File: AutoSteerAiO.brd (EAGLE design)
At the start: 114.3 x 99.1 mm, 81 parts, among them IC2 MMA8452Q, J4 CONNECTOR 1x5 PINS, K4 CB1A-P-12V

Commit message: Add files via upload
silkscreen edit
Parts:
- moved D3 1.91 mm to (36.2, 90.8)
- moved D2 0.63 mm to (42.5, 90.8)
- moved INT 0.45 mm to (27.3, 80.6)
- moved PCB1 0.44 mm to (48.1, 32.4)
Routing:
- net GND: track 460.9 -> 463.2 mm, vias 85 -> 79
- net N$26: track 77.2 -> 75.7 mm
- net SDA: track 98.8 -> 97.9 mm
- net SCL: track 99.0 -> 98.1 mm

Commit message: Add files via upload
silkscreen edit
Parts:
- moved C11 0.64 mm to (42.5, 65.4)
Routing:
- net +15V: track 131.5 -> 127.8 mm
- net +5V: track 233.9 -> 232.1 mm
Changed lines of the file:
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@@
 <drawing>
 <settings>
-<setting alwaysvectorfont="yes"/>
+<setting alwaysvectorfont="no"/>
 <setting keepoldvectorfont="yes"/>
 <setting verticaltext="up"/>
@@
 <text x="39.37" y="30.226" size="1.016" layer="25" font="vector" ratio="12" rot="R180" align="center">USB</text>
 <text x="40.64" y="114.3" size="2.54" layer="25" font="vector" ratio="14" rot="R180" align="center">AGOpenGPS</text>
-<text x="41.91" y="61.595" size="0.8128" layer="25" font="vector" ratio="12" rot="R180" align="center">.1uF</text>
+<text x="42.545" y="61.595" size="0.8128" layer="25" font="vector" ratio="12" rot="R180" align="center">.1uF</text>
 <text x="54.61" y="33.02" size="0.7112" layer="25" font="vector" ratio="10" align="center">3V</text>
 <text x="67.31" y="33.02" size="0.7112" layer="25" font="vector" ratio="10" align="center">GND</text>
@@
 <attribute name="OC_NEWARK" value="unknown" x="116.84" y="114.3" size="1.778" layer="27" display="off"/>
 </element>
-<element name="C11" library="resistor" library_urn="urn:adsk.eagle:library:348" package="C050-024X044" package3d_urn="urn:adsk.eagle:package:23643/1" value=".1uF" x="41.91" y="65.405" smashed="yes" rot="R270">
-<attribute name="MF" value="" x="41.91" y="65.405" size="1.778" layer="27" rot="R270" display="off"/>
-<attribute name="MPN" value="" x="41.91" y="65.405" size="1.778" layer="27" rot="R270" display="off"/>
-<attribute name="NAME" x="41.91" y="69.215" size="0.8128" layer="25" font="vector" ratio="12" rot="R180" align="center"/>
-<attribute name="OC_NEWARK" value="unknown" x="41.91" y="65.405" size="1.778" layer="27" rot="R270" display="off"/>
+<element name="C11" library="resistor" library_urn="urn:adsk.eagle:library:348" package="C050-024X044" package3d_urn="urn:adsk.eagle:package:23643/1" value=".1uF" x="42.545" y="65.405" smashed="yes" rot="R270">
+<attribute name="MF" value="" x="42.545" y="65.405" size="1.778" layer="27" rot="R270" display="off"/>
+<attribute name="MPN" value="" x="42.545" y="65.405" size="1.778" layer="27" rot="R270" display="off"/>
+<attribute name="NAME" x="42.545" y="69.215" size="0.8128" layer="25" font="vector" ratio="12" rot="R180" align="center"/>
+<attribute name="OC_NEWARK" value="unknown" x="42.545" y="65.405" size="1.778" layer="27" rot="R270" display="off"/>
 </element>
 <element name="C12" library="resistor" library_urn="urn:adsk.eagle:library:348" package="C050-024X044" package3d_urn="urn:adsk.eagle:package:23643/1" value=".1uF" x="50.8" y="33.655" smashed="yes" rot="R270">
@@
 <attribute name="CYTRON-PC" value="CN-2600PS-05" x="117.475" y="68.58" size="1.778" layer="27" rot="R90" display="off"/>
 <attribute name="DESC" value="2600 PCB Connector" x="117.475" y="68.58" size="1.778" layer="27" rot="R90" display="off"/>
+<attribute name="LABEL" value="" x="120.396" y="67.183" size="0.762" layer="51" font="vector" ratio="15" rot="R90" align="top-left"/>
 <attribute name="LABEL" value="" x="120.396" y="67.183" size="0.762" layer="21" font="vector" ratio="15" rot="R90" align="top-left"/>
-<attribute name="LABEL" value="" x="120.396" y="67.183" size="0.762" layer="51" font="vector" ratio="15" rot="R90" align="top-left"/>
 <attribute name="LABEL" value="" x="117.475" y="68.58" size="1.778" layer="27" rot="R90" display="off"/>
 <attribute name="MF" value="" x="117.475" y="68.58" size="1.778" layer="27" rot="R90" display="off"/>
@@
 <contactref element="+5V1" pad="1"/>
 <wire x1="10.16" y1="31.3055" x2="10.16" y2="70.8025" width="0.6096" layer="1"/>
-<wire x1="41.91" y1="36.83" x2="41.91" y2="62.865" width="0.6096" layer="1"/>
-<wire x1="41.91" y1="36.83" x2="30.48" y2="25.4" width="0.6096" layer="1"/>
-<wire x1="46.7995" y1="62.865" x2="41.91" y2="62.865" width="0.508" layer="1"/>
+<wire x1="42.545" y1="37.465" x2="42.545" y2="62.865" width="0.6096" layer="1"/>
+<wire x1="42.545" y1="37.465" x2="30.48" y2="25.4" width="0.6096" layer="1"/>
+<wire x1="46.7995" y1="62.865" x2="42.545" y2="62.865" width="0.508" layer="1"/>
 <contactref element="PS2" pad="3"/>
 <contactref element="C10" pad="2"/>
@@
 <wire x1="14.9225" y1="75.565" x2="10.16" y2="70.8025" width="0.6096" layer="1"/>
 <wire x1="15.0013125" y1="88.9" x2="12.7" y2="88.9" width="0.4064" layer="1"/>
-<wire x1="18.6081125" y1="92.5068" x2="15.0013125" y2="88.9" width="0.4064" layer="1"/>
-<wire x1="51.435" y1="80.01" x2="38.9382" y2="92.5068" width="0.4064" layer="1"/>
-<wire x1="38.9382" y1="92.5068" x2="18.6081125" y2="92.5068" width="0.4064" layer="1"/>
+<wire x1="16.9063125" y1="90.805" x2="15.0013125" y2="88.9" width="0.4064" layer="1"/>
+<wire x1="50.165" y1="80.01" x2="39.37" y2="90.805" width="0.4064" layer="1"/>
+<wire x1="39.37" y1="90.805" x2="16.9063125" y2="90.805" width="0.4064" layer="1"/>
 <wire x1="61.9125" y1="80.01" x2="63.5" y2="81.5975" width="0.4064" layer="1"/>
-<wire x1="51.435" y1="80.01" x2="61.9125" y2="80.01" width="0.4064" layer="1"/>
+<wire x1="50.165" y1="80.01" x2="61.9125" y2="80.01" width="0.4064" layer="1"/>
 <contactref element="C16" pad="+"/>
 <wire x1="12.7" y1="85.09" x2="20.28" y2="85.09" width="0.8128" layer="1"/>
@@
 <via x="15.24" y="57.15" extent="1-16" drill="0.508"/>
 <via x="16.51" y="22.86" extent="1-16" drill="0.508"/>
-<via x="33.655" y="50.8" extent="1-16" drill="0.508"/>
+<via x="33.655" y="48.895" extent="1-16" drill="0.508"/>
 <via x="58.42" y="25.4" extent="1-16" drill="0.508"/>
-<via x="39.37" y="78.105" extent="1-16" drill="0.508"/>
+<via x="39.37" y="78.74" extent="1-16" drill="0.508"/>
 <contactref element="J4" pad="1"/>
 <contactref element="JP1" pad="1"/>
@@
 <wire x1="117.475" y1="68.58" x2="120.015" y2="68.58" width="0.6096" layer="16"/>
 <wire x1="117.475" y1="85.09" x2="120.015" y2="85.09" width="0.6096" layer="16"/>
-<via x="38.735" y="36.83" extent="1-16" drill="0.508"/>
-<via x="38.735" y="22.86" extent="1-16" drill="0.508"/>
+<via x="39.37" y="36.83" extent="1-16" drill="0.508"/>
+<via x="39.37" y="22.86" extent="1-16" drill="0.508"/>
 <polygon width="0" layer="16" isolate="0.3556" thermals="no">
 <vertex x="120.65" y="63.5"/>
@@
 <vertex x="120.65" y="30.48"/>
 </polygon>
-<wire x1="46.7995" y1="67.945" x2="41.91" y2="67.945" width="0.6096" layer="16"/>
-<wire x1="41.91" y1="67.945" x2="36.83" y2="62.865" width="0.6096" layer="16"/>
-<wire x1="36.83" y1="62.865" x2="31.5595" y2="62.865" width="0.6096" layer="16"/>
+<wire x1="46.7995" y1="67.945" x2="42.545" y2="67.945" width="0.6096" layer="16"/>
+<wire x1="42.545" y1="67.945" x2="37.465" y2="62.865" width="0.6096" layer="16"/>
+<wire x1="37.465" y1="62.865" x2="31.5595" y2="62.865" width="0.6096" layer="16"/>
 <wire x1="31.5595" y1="62.865" x2="31.5341" y2="62.8904" width="0.6096" layer="16"/>
 <wire x1="31.5341" y1="62.8904" x2="22.8854" y2="62.8904" width="0.6096" layer="16"/>
@@
 <wire x1="67.31" y1="36.195" x2="50.8" y2="36.195" width="0.6096" layer="16"/>
 <wire x1="67.31" y1="31.115" x2="67.31" y2="36.195" width="0.6096" layer="16"/>
-<via x="43.815" y="50.8" extent="1-16" drill="0.508"/>
+<via x="44.45" y="48.895" extent="1-16" drill="0.508"/>
 <via x="113.03" y="22.86" extent="1-16" drill="0.508"/>
 <via x="40.64" y="111.125" extent="1-16" drill="0.508"/>
@@
 <wire x1="16.51" y1="60.325" x2="16.51" y2="67.945" width="0.508" layer="1"/>
 <wire x1="16.51" y1="67.945" x2="17.78" y2="69.215" width="0.508" layer="1"/>
-<wire x1="42.545" y1="85.725" x2="38.2016" y2="90.0684" width="0.8128" layer="1"/>
-<wire x1="38.2016" y1="90.0684" x2="25.3297125" y2="90.0684" width="0.8128" layer="1"/>
-<wire x1="25.3297125" y1="90.0684" x2="23.495" y2="88.2336875" width="0.8128" layer="1"/>
+<wire x1="42.545" y1="85.725" x2="40.64" y2="87.63" width="0.8128" layer="1"/>
+<wire x1="40.64" y1="87.63" x2="25.7488125" y2="87.63" width="0.8128" layer="1"/>
+<wire x1="25.7488125" y1="87.63" x2="23.495" y2="85.3761875" width="0.8128" layer="1"/>
 <polygon width="0" layer="16" thermals="no">
 <vertex x="74.295" y="85.09"/>
@@
 <vertex x="86.995" y="85.09"/>
 </polygon>
-<wire x1="23.495" y1="88.2336875" x2="23.495" y2="73.66" width="0.8128" layer="1"/>
+<wire x1="23.495" y1="85.3761875" x2="23.495" y2="73.66" width="0.8128" layer="1"/>
 <wire x1="23.495" y1="73.66" x2="21.2725" y2="73.66" width="0.6096" layer="1"/>
 <wire x1="21.2725" y1="73.66" x2="17.78" y2="70.1675" width="0.6096" layer="1"/>

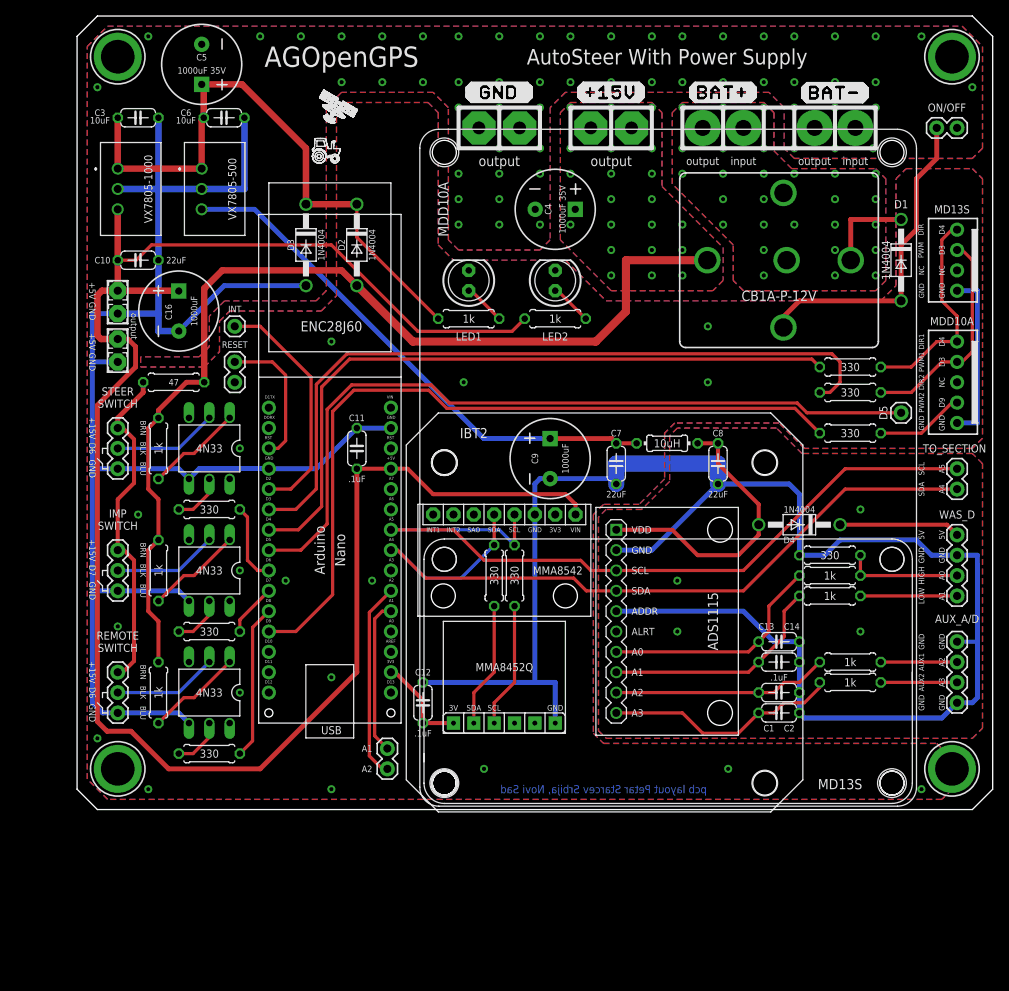
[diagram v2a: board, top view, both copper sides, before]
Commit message: Add files via upload
Added MD10C driver
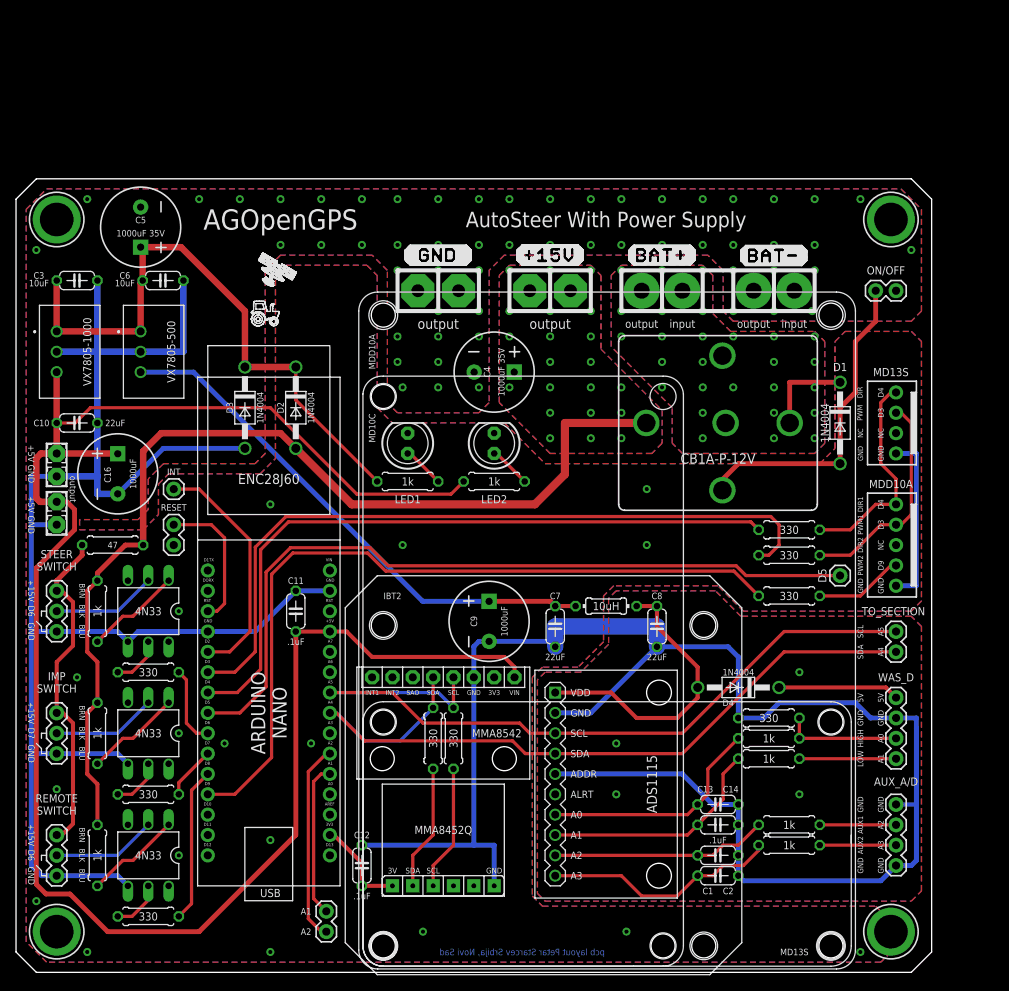
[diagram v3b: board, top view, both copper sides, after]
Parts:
- added U$3: MD10C, #Motor Drivers:MD10C
- moved U$1 99.4 mm to (45.8, 3.30), turned to 90 degrees
- moved +5V 21.7 mm to (5.08, 58.7)
- moved +5V1 21.7 mm to (5.08, 64.8)
- moved C10 21.7 mm to (7.62, 68.6)
- moved C3 21.7 mm to (7.62, 86.4)
- moved C6 21.7 mm to (18.4, 86.4)
- moved C9 21.7 mm to (59.1, 43.8)
- moved D1 21.7 mm to (102.9, 68.6)
- moved D2 21.7 mm to (34.9, 70.5)
- moved D3 21.7 mm to (28.6, 70.5)
- moved JP1 21.7 mm to (109.9, 68.6)
- moved K4 21.7 mm to (87.6, 68.6)
- moved L1 21.7 mm to (73.7, 45.7)
- moved PS1 21.7 mm to (16.8, 77.5)
- moved PS2 21.7 mm to (6.35, 77.5)
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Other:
- board text added: "MD10C"
- board text removed: "ENC28J60"

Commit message: Add files via upload
added MD10C holes
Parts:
- moved R10 0.64 mm to (94.0, 26.0)
- moved R11 0.64 mm to (94.0, 28.6)
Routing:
- net HIGH.: track 14.6 -> 15.5 mm
- net LOW: track 28.7 -> 28.0 mm
- net HIGH: track 28.7 -> 28.0 mm
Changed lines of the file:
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@@
 <drawing>
 <settings>
-<setting alwaysvectorfont="yes"/>
+<setting alwaysvectorfont="no"/>
 <setting keepoldvectorfont="yes"/>
 <setting verticaltext="up"/>
 </settings>
-<grid distance="50" unitdist="mil" unit="mm" style="lines" multiple="1" display="no" altdistance="5" altunitdist="mil" altunit="mil"/>
+<grid distance="50" unitdist="mil" unit="mil" style="lines" multiple="1" display="yes" altdistance="25" altunitdist="mil" altunit="mil"/>
 <layers>
 <layer number="1" name="Top" color="4" fill="1" visible="yes" active="yes"/>
@@
 <attribute name="VALUE" x="96.52" y="52.07" size="1.016" layer="25" font="vector" ratio="12" rot="R180" align="center"/>
 </element>
-<element name="R10" library="resistor" library_urn="urn:adsk.eagle:library:348" package="0207/7" package3d_urn="urn:adsk.eagle:package:23493/2" value="1k" x="93.98" y="26.67" smashed="yes" rot="R180">
-<attribute name="MF" value="" x="93.98" y="26.67" size="1.778" layer="27" rot="R180" display="off"/>
-<attribute name="MPN" value="" x="93.98" y="26.67" size="1.778" layer="27" rot="R180" display="off"/>
-<attribute name="OC_NEWARK" value="unknown" x="93.98" y="26.67" size="1.778" layer="27" rot="R180" display="off"/>
-<attribute name="VALUE" x="93.98" y="26.67" size="1.016" layer="25" font="vector" ratio="12" align="center"/>
-</element>
-<element name="R11" library="resistor" library_urn="urn:adsk.eagle:library:348" package="0207/7" package3d_urn="urn:adsk.eagle:package:23493/2" value="1k" x="93.98" y="29.21" smashed="yes" rot="R180">
-<attribute name="MF" value="" x="93.98" y="29.21" size="1.778" layer="27" rot="R180" display="off"/>
-<attribute name="MPN" value="" x="93.98" y="29.21" size="1.778" layer="27" rot="R180" display="off"/>
-<attribute name="OC_NEWARK" value="unknown" x="93.98" y="29.21" size="1.778" layer="27" rot="R180" display="off"/>
-<attribute name="VALUE" x="93.98" y="29.21" size="1.016" layer="25" font="vector" ratio="12" align="center"/>
+<element name="R10" library="resistor" library_urn="urn:adsk.eagle:library:348" package="0207/7" package3d_urn="urn:adsk.eagle:package:23493/2" value="1k" x="93.98" y="26.035" smashed="yes" rot="R180">
+<attribute name="MF" value="" x="93.98" y="26.035" size="1.778" layer="27" rot="R180" display="off"/>
+<attribute name="MPN" value="" x="93.98" y="26.035" size="1.778" layer="27" rot="R180" display="off"/>
+<attribute name="OC_NEWARK" value="unknown" x="93.98" y="26.035" size="1.778" layer="27" rot="R180" display="off"/>
+<attribute name="VALUE" x="93.98" y="26.035" size="1.016" layer="25" font="vector" ratio="12" align="center"/>
+</element>
+<element name="R11" library="resistor" library_urn="urn:adsk.eagle:library:348" package="0207/7" package3d_urn="urn:adsk.eagle:package:23493/2" value="1k" x="93.98" y="28.575" smashed="yes" rot="R180">
+<attribute name="MF" value="" x="93.98" y="28.575" size="1.778" layer="27" rot="R180" display="off"/>
+<attribute name="MPN" value="" x="93.98" y="28.575" size="1.778" layer="27" rot="R180" display="off"/>
+<attribute name="OC_NEWARK" value="unknown" x="93.98" y="28.575" size="1.778" layer="27" rot="R180" display="off"/>
+<attribute name="VALUE" x="93.98" y="28.575" size="1.016" layer="25" font="vector" ratio="12" align="center"/>
 </element>
 <element name="R6" library="resistor" library_urn="urn:adsk.eagle:library:348" package="0207/7" package3d_urn="urn:adsk.eagle:package:23493/2" value="330" x="52.07" y="29.21" smashed="yes" rot="R90">
@@
 <attribute name="CYTRON-PC" value="CN-2600PS-05" x="109.855" y="48.26" size="1.778" layer="27" rot="R90" display="off"/>
 <attribute name="DESC" value="2600 PCB Connector" x="109.855" y="48.26" size="1.778" layer="27" rot="R90" display="off"/>
+<attribute name="LABEL" value="" x="112.776" y="46.863" size="0.762" layer="51" font="vector" ratio="15" rot="R90" align="top-left"/>
 <attribute name="LABEL" value="" x="112.776" y="46.863" size="0.762" layer="21" font="vector" ratio="15" rot="R90" align="top-left"/>
-<attribute name="LABEL" value="" x="112.776" y="46.863" size="0.762" layer="51" font="vector" ratio="15" rot="R90" align="top-left"/>
 <attribute name="LABEL" value="" x="109.855" y="48.26" size="1.778" layer="27" rot="R90" display="off"/>
 <attribute name="MF" value="" x="109.855" y="48.26" size="1.778" layer="27" rot="R90" display="off"/>
@@
 <contactref element="R11" pad="1"/>
 <contactref element="R4" pad="1"/>
-<wire x1="97.79" y1="29.21" x2="109.855" y2="29.21" width="0.4064" layer="1"/>
-<wire x1="97.79" y1="31.75" x2="97.79" y2="29.21" width="0.4064" layer="1"/>
+<wire x1="107.95" y1="28.575" x2="97.79" y2="28.575" width="0.4064" layer="1"/>
+<wire x1="108.585" y1="29.21" x2="109.855" y2="29.21" width="0.4064" layer="1"/>
+<wire x1="108.585" y1="29.21" x2="107.95" y2="28.575" width="0.4064" layer="1"/>
+<wire x1="97.79" y1="31.75" x2="97.79" y2="28.575" width="0.4064" layer="1"/>
 </signal>
 <signal name="LOW.">
 <contactref element="WAS_D" pad="4"/>
 <contactref element="R10" pad="1"/>
-<wire x1="109.855" y1="26.67" x2="97.79" y2="26.67" width="0.4064" layer="1"/>
+<wire x1="109.855" y1="26.67" x2="108.585" y2="26.67" width="0.4064" layer="1"/>
+<wire x1="108.585" y1="26.67" x2="107.95" y2="26.035" width="0.4064" layer="1"/>
+<wire x1="107.95" y1="26.035" x2="97.79" y2="26.035" width="0.4064" layer="1"/>
 </signal>
 <signal name="GND">
@@
 <contactref element="R11" pad="2"/>
 <contactref element="C14" pad="2"/>
-<wire x1="90.17" y1="29.21" x2="86.36" y2="25.4" width="0.4064" layer="1"/>
-<wire x1="86.36" y1="25.4" x2="86.36" y2="22.225" width="0.4064" layer="1"/>
+<wire x1="90.17" y1="28.575" x2="86.36" y2="24.765" width="0.4064" layer="1"/>
+<wire x1="86.36" y1="24.765" x2="86.36" y2="22.225" width="0.4064" layer="1"/>
 <wire x1="86.36" y1="22.225" x2="85.09" y2="20.955" width="0.4064" layer="1"/>
 <wire x1="85.09" y1="20.955" x2="83.82" y2="19.685" width="0.4064" layer="1"/>
@@
 <wire x1="67.31" y1="17.145" x2="83.82" y2="17.145" width="0.4064" layer="1"/>
 <wire x1="83.82" y1="17.145" x2="85.09" y2="18.415" width="0.4064" layer="1"/>
-<wire x1="90.17" y1="26.67" x2="88.265" y2="24.765" width="0.4064" layer="1"/>
-<wire x1="88.265" y1="24.765" x2="88.265" y2="21.59" width="0.4064" layer="1"/>
+<wire x1="90.17" y1="26.035" x2="88.265" y2="24.13" width="0.4064" layer="1"/>
+<wire x1="88.265" y1="24.13" x2="88.265" y2="21.59" width="0.4064" layer="1"/>
 <wire x1="88.265" y1="21.59" x2="85.09" y2="18.415" width="0.4064" layer="1"/>
 </signal>
